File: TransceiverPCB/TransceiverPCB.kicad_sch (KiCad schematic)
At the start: 67 parts, among them IC1 QPL6220QTR7, IC2 AD9218BSTZ-65, IC3 AD9763ASTZ, IC4 ADF4351BCPZ-RL7, J1 USB4085-GF-A_REVB, J2 RFPC-SMA27-F, J3 RFPC-SMA27-F, SW1 SW_Push, SW2 SW_Push, U1 XC7A35T-1FTG256C, U10 AP2112K-3.3TRG1, U11 LM66100DCKR, U12 ADL5387ACPZ-R7, U2 W25Q32JVSSIQ, U3 W25Q32JVSSIQ, U4 DSC1001CI2-100.0000T, U5 ADL5380ACPZ-R7, U6 ADL5375-05ACPZ-R7, U7 ADA4940-2ACPZ-R7, U8 ADL5320ARKZ-R7, U9 SC09147, X1 ABM8-272-T3

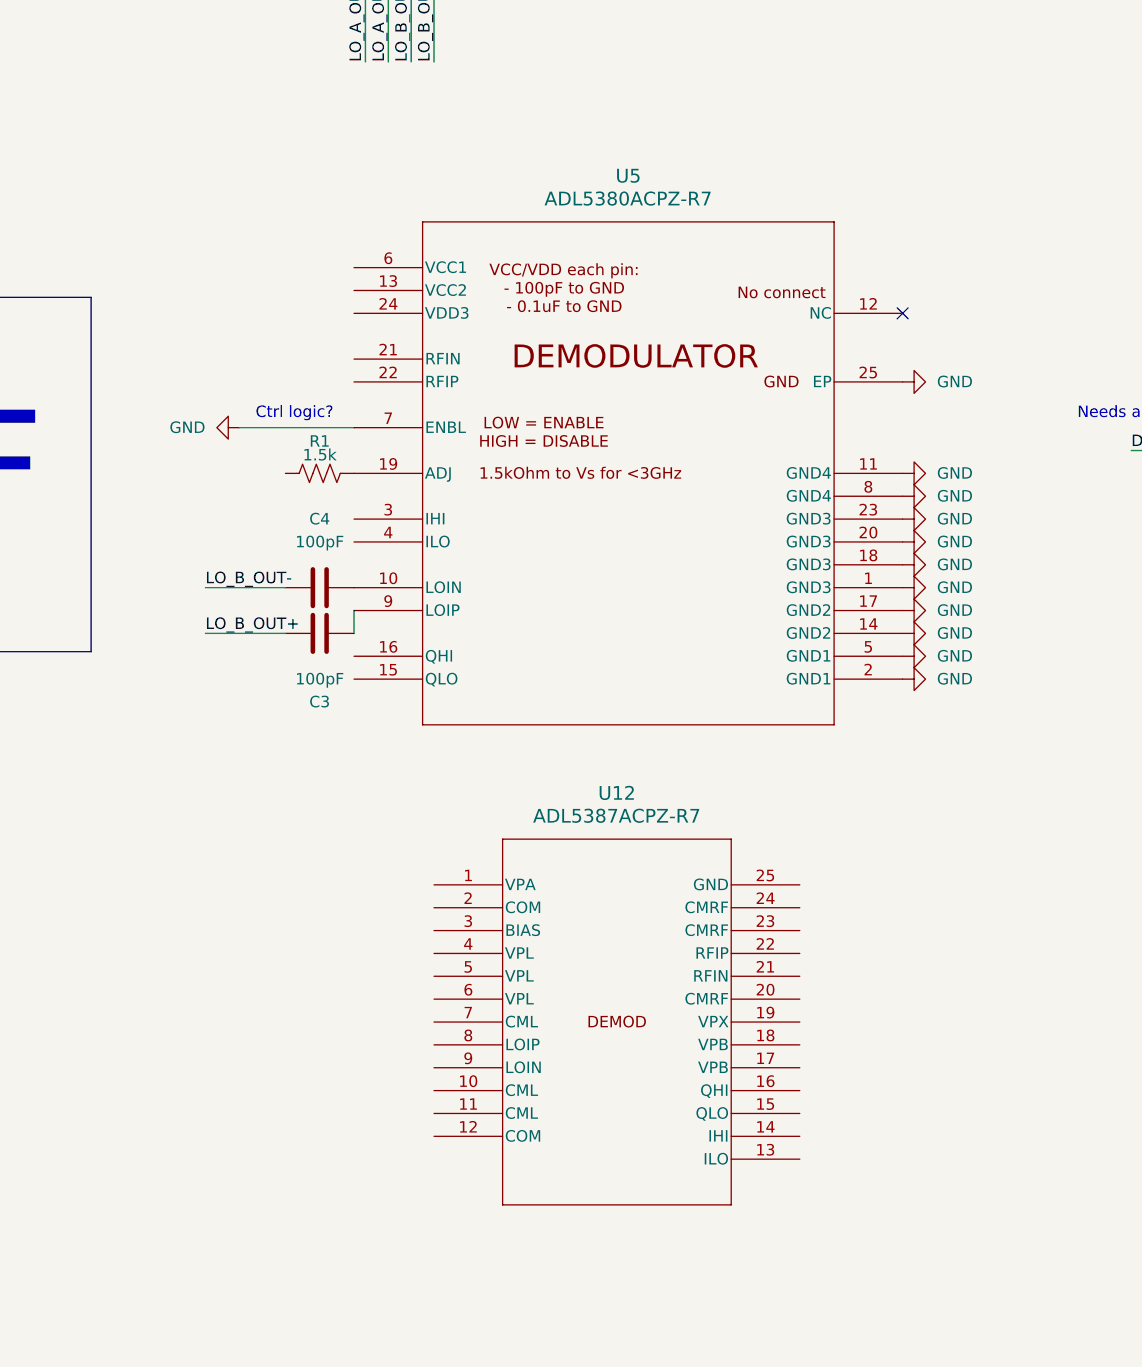
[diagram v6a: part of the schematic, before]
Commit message: Removed old DEMOD
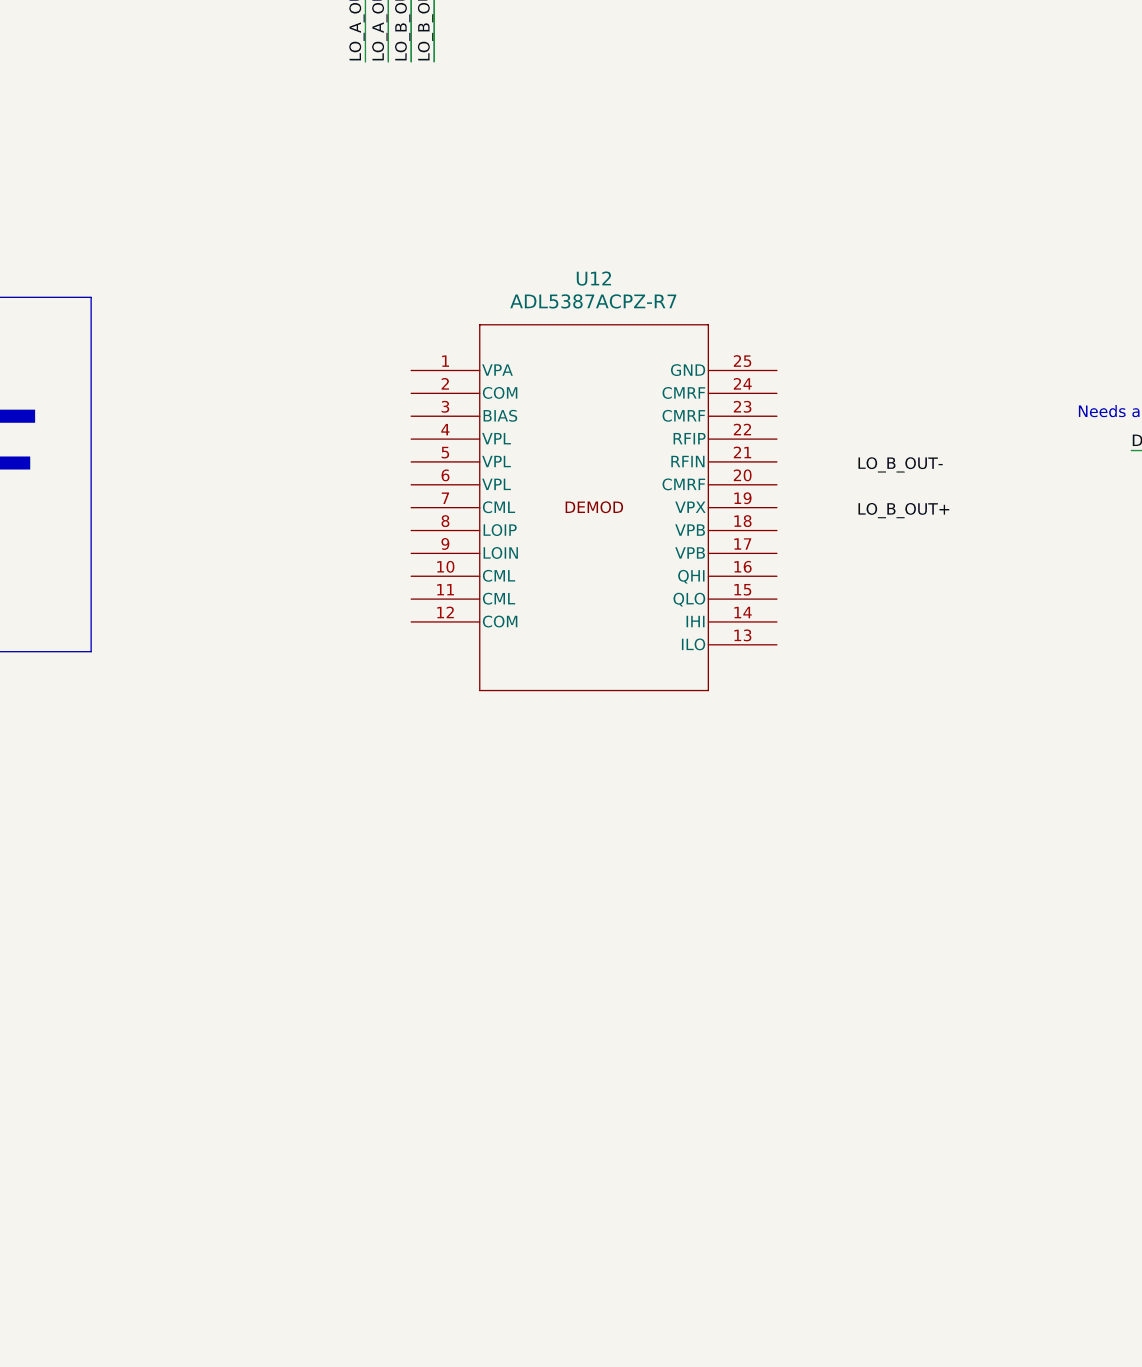
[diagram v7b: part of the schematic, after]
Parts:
- removed C3, C4: 100pF, symbol Device:C
- removed R1: 1.5k, symbol Device:R_US
- removed U5: ADL5380ACPZ-R7, CP_24_3_ADI, symbol LIB_IRISHSAT:ADL5380ACPZ-R7
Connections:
- no-connect marks 48 -> 47
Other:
- moved on the sheet: U12

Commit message: Added some SPI on FPGA and RP2040
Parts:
- added C3, C4: 100pF, symbol Device:C
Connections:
- net +3V3: now also U1.P7 (VCCO_14), U1.T11 (VCCO_14)
- net GND: now also U1.A1 (GND), U1.A11 (GND), U1.B8 (GND), U1.C15 (GND), U1.C5 (GND), U1.D12 (GND), U1.D2 (GND), U1.E9 (GND), U1.F10 (GND), U1.F16 (GND), U1.F6 (GND), U1.G13 (GND), U1.G3 (GND), U1.G9 (GND), U1.H6 (GND), U1.K4 (GND), U1.K6 (GND), U1.L1 (GND), U1.L11 (GND), U1.M8 (GND), U1.N15 (GND), U1.N5 (GND), U1.P12 (GND), U1.P2 (GND), U1.R9 (GND), U1.T16 (GND), U1.T6 (GND)
- net LO_B_OUT+: now also C3.1
- net LO_B_OUT-: now also C4.1
- net SPI0_SCK_RP2040_FPGA: now reaches U9.4 (GPIO2)
- net SPI0_SCK_RP2040_FPGA: now also U1.N14 (IO_L12P_T1_MRCC_14)
- net SPI0_MOSI_RP2040_FPGA: now reaches U9.5 (GPIO3)
- net SPI0_MOSI_RP2040_FPGA: now also U1.N12 (IO_L13N_T2_MRCC_14)
- net SPI0_MISO_RP2040_FPGA: now reaches U9.6 (GPIO4)
- net SPI0_MISO_RP2040_FPGA: now also U1.N11 (IO_L13P_T2_MRCC_14)
- net SPI0_CS_RP2040_FPGA: now reaches U9.7 (GPIO5)
- net SPI0_CS_RP2040_FPGA: now also U1.N13 (IO_L11P_T1_SRCC_14)
- net at U12.8 (LOIP): now also C3.2
- net at U12.9 (LOIN): now also C4.2
- no-connect marks 47 -> 43
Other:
- note added: "Decoupling C?"
- moved on the sheet: C9, IC2, R2, R5, SW2, U3, U7
